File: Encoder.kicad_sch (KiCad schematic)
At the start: 6 parts, among them J2 ABZ encoder, J3 I2C ENCODER, J4 Conn_01x06_Male, J5 ANALOG ENCODER, U3 AS5055A

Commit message: finished routing
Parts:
- removed U3: AS5055A, Package_DFN_QFN:QFN-16-1EP_4x4mm_P0.65mm_EP2.7x2.7mm_PullBack, symbol Sensor_Magnetic:AS5055A
- added U3: AS5048B, Package_SO:TSSOP-14_4.4x5mm_P0.65mm, symbol Sensor_Magnetic:AS5048B
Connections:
- net +3.3V: now also U3.11 (VDD5V), U3.12 (VDD3V)
- net A: now also J2.5 (Pin_5); no longer J2.3 (Pin_3)
- net GND: now also U3.13 (GND), U3.3 (A2), U3.4 (A1)
- net I2C_SCL: now also J3.3 (Pin_3), U3.2 (SCL); no longer J3.4 (Pin_4)
- net I2C_SDA: now also J3.4 (Pin_4), U3.1 (SDA); no longer J3.3 (Pin_3)
- net Z: now also J2.3 (Pin_3); no longer J2.5 (Pin_5)
- new net ENC_PWM: U3.14 (PWM)
- no-connect marks 0 -> 6
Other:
- moved on the sheet: C32

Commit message: Routing done
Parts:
- added R11, R12: 10K, Resistor_SMD:R_0402_1005Metric, symbol Device:R
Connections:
- net +3.3V: now also R11.2, R12.2
- net I2C_SCL: now also R11.1
- net I2C_SDA: now also R12.1
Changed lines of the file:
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@@
     (effects (font (size 1.27 1.27)) (justify left))
   )
+  (hierarchical_label "I2C_SDA" (shape output) (at 159.766 160.274 180)
+    (effects (font (size 1.27 1.27)) (justify right))
+  )
   (hierarchical_label "ANALOG" (shape output) (at 126.238 47.244 270)
     (effects (font (size 1.27 1.27)) (justify right))
@@
     (effects (font (size 1.27 1.27)) (justify right))
   )
+  (hierarchical_label "I2C_SCL" (shape output) (at 159.766 157.734 180)
+    (effects (font (size 1.27 1.27)) (justify right))
+  )
   (hierarchical_label "I2C_SDA" (shape output) (at 87.122 66.04 270)
     (effects (font (size 1.27 1.27)) (justify right))
@@
   (hierarchical_label "SPI_CS" (shape input) (at 92.71 89.154 270)
     (effects (font (size 1.27 1.27)) (justify right))
+  )
+  (symbol (lib_id "Device:R") (at 163.576 157.734 90) (unit 1)
+    (in_bom yes) (on_board yes)
+    (property "Reference" "R11" (id 0) (at 164.338 157.988 90)
+      (effects (font (size 1.27 1.27)) (justify left))
+    )
+    (property "Value" "10K" (id 1) (at 165.1 155.956 90)
+      (effects (font (size 1.27 1.27)) (justify left))
+    )
+    (property "Footprint" "Resistor_SMD:R_0402_1005Metric" (id 2) (at 163.576 159.512 90)
+      (effects (font (size 1.27 1.27)) hide)
+    )
+    (property "Datasheet" "~" (id 3) (at 163.576 157.734 0)
+      (effects (font (size 1.27 1.27)) hide)
+    )
+    (pin "1")
+    (pin "2")
   )
   (symbol (lib_id "power:GND") (at 182.372 119.126 0) (unit 1)
@@
     (pin "2")
   )
+  (symbol (lib_id "Device:R") (at 163.576 160.274 90) (unit 1)
+    (in_bom yes) (on_board yes)
+    (property "Reference" "R12" (id 0) (at 164.338 160.528 90)
+      (effects (font (size 1.27 1.27)) (justify left))
+    )
+    (property "Value" "10K" (id 1) (at 164.846 162.052 90)
+      (effects (font (size 1.27 1.27)) (justify left))
+    )
+    (property "Footprint" "Resistor_SMD:R_0402_1005Metric" (id 2) (at 163.576 162.052 90)
+      (effects (font (size 1.27 1.27)) hide)
+    )
+    (property "Datasheet" "~" (id 3) (at 163.576 160.274 0)
+      (effects (font (size 1.27 1.27)) hide)
+    )
+    (pin "1")
+    (pin "2")
+  )
   (symbol (lib_id "power:GND") (at 167.386 125.476 270) (unit 1)
     (in_bom yes) (on_board yes) (fields_autoplaced)
@@
     )
     (property "Datasheet" "" (id 3) (at 97.79 89.154 0)
+      (effects (font (size 1.27 1.27)) hide)
+    )
+    (pin "1")
+  )
+  (symbol (lib_id "power:+3.3V") (at 167.386 157.734 270) (unit 1)
+    (in_bom yes) (on_board yes) (fields_autoplaced)
+    (property "Reference" "#PWR0126" (id 0) (at 163.576 157.734 0)
+      (effects (font (size 1.27 1.27)) hide)
+    )
+    (property "Value" "+3.3V" (id 1) (at 171.45 157.7339 90)
+      (effects (font (size 1.27 1.27)) (justify left))
+    )
+    (property "Footprint" "" (id 2) (at 167.386 157.734 0)
+      (effects (font (size 1.27 1.27)) hide)
+    )
+    (property "Datasheet" "" (id 3) (at 167.386 157.734 0)
       (effects (font (size 1.27 1.27)) hide)
     )
@@
       (effects (font (size 1.27 1.27)) hide)
     )
+    (pin "1")
+  )
+  (symbol (lib_id "power:+3.3V") (at 167.386 160.274 270) (unit 1)
+    (in_bom yes) (on_board yes) (fields_autoplaced)
+    (property "Reference" "#PWR0127" (id 0) (at 163.576 160.274 0)
+      (effects (font (size 1.27 1.27)) hide)
+    )
+    (property "Value" "+3.3V" (id 1) (at 171.45 160.2739 90)
+      (effects (font (size 1.27 1.27)) (justify left))
+    )
+    (property "Footprint" "" (id 2) (at 167.386 160.274 0)
+      (effects (font (size 1.27 1.27)) hide)
+    )
+    (property "Datasheet" "" (id 3) (at 167.386 160.274 0)
+      (effects (font (size 1.27 1.27)) hide)
+    )

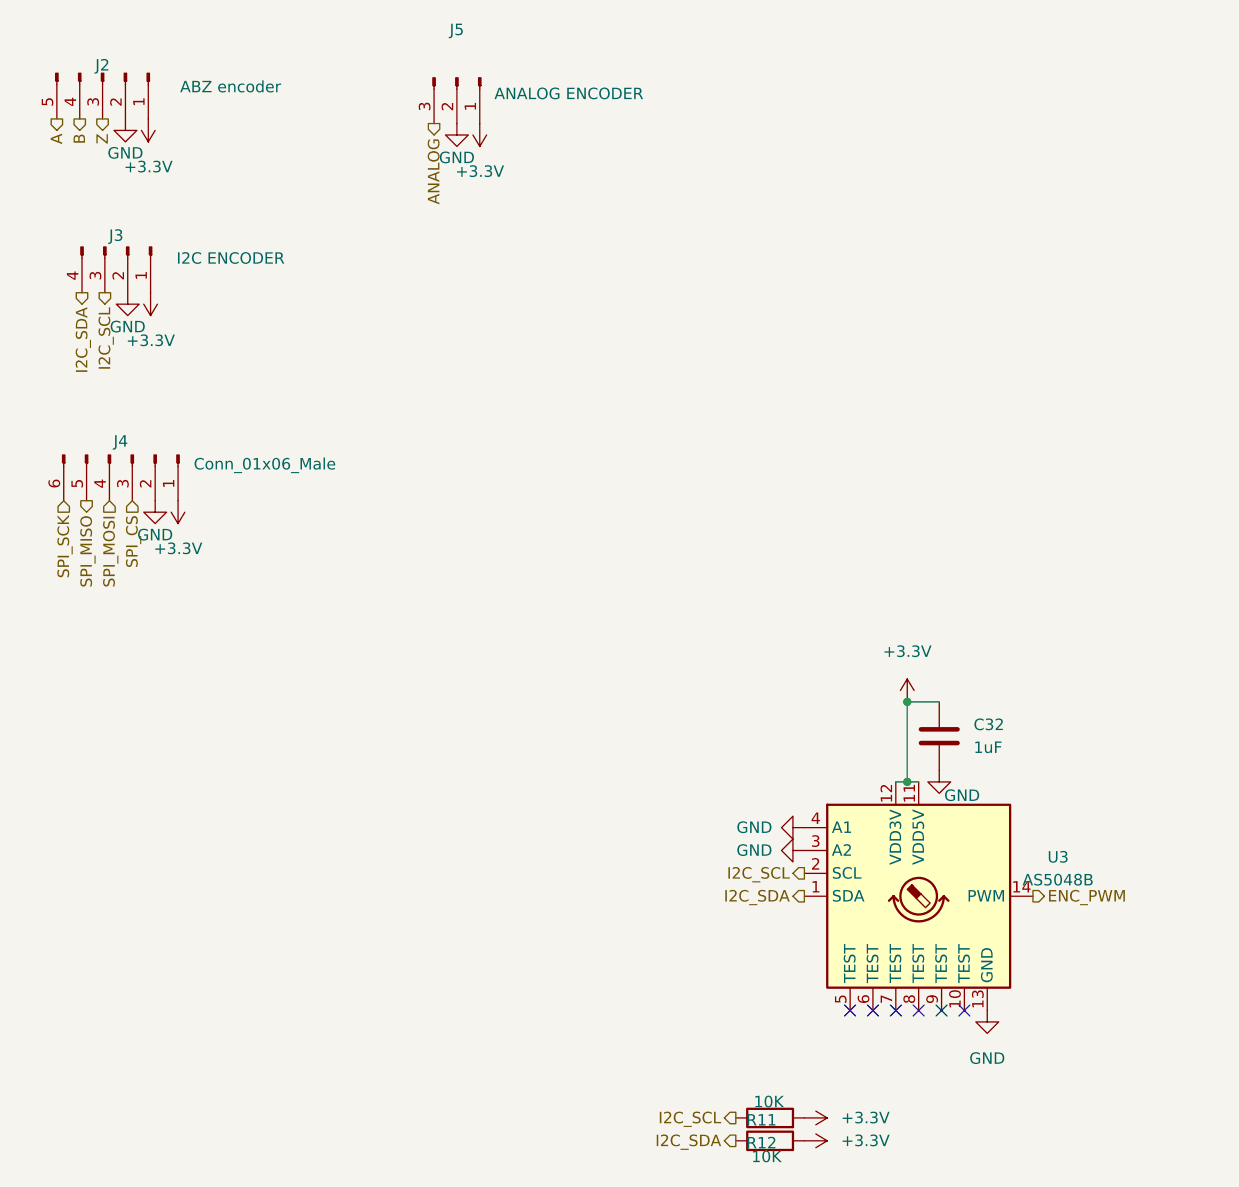
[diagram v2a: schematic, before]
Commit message: Using DRV8353 with built in current sense
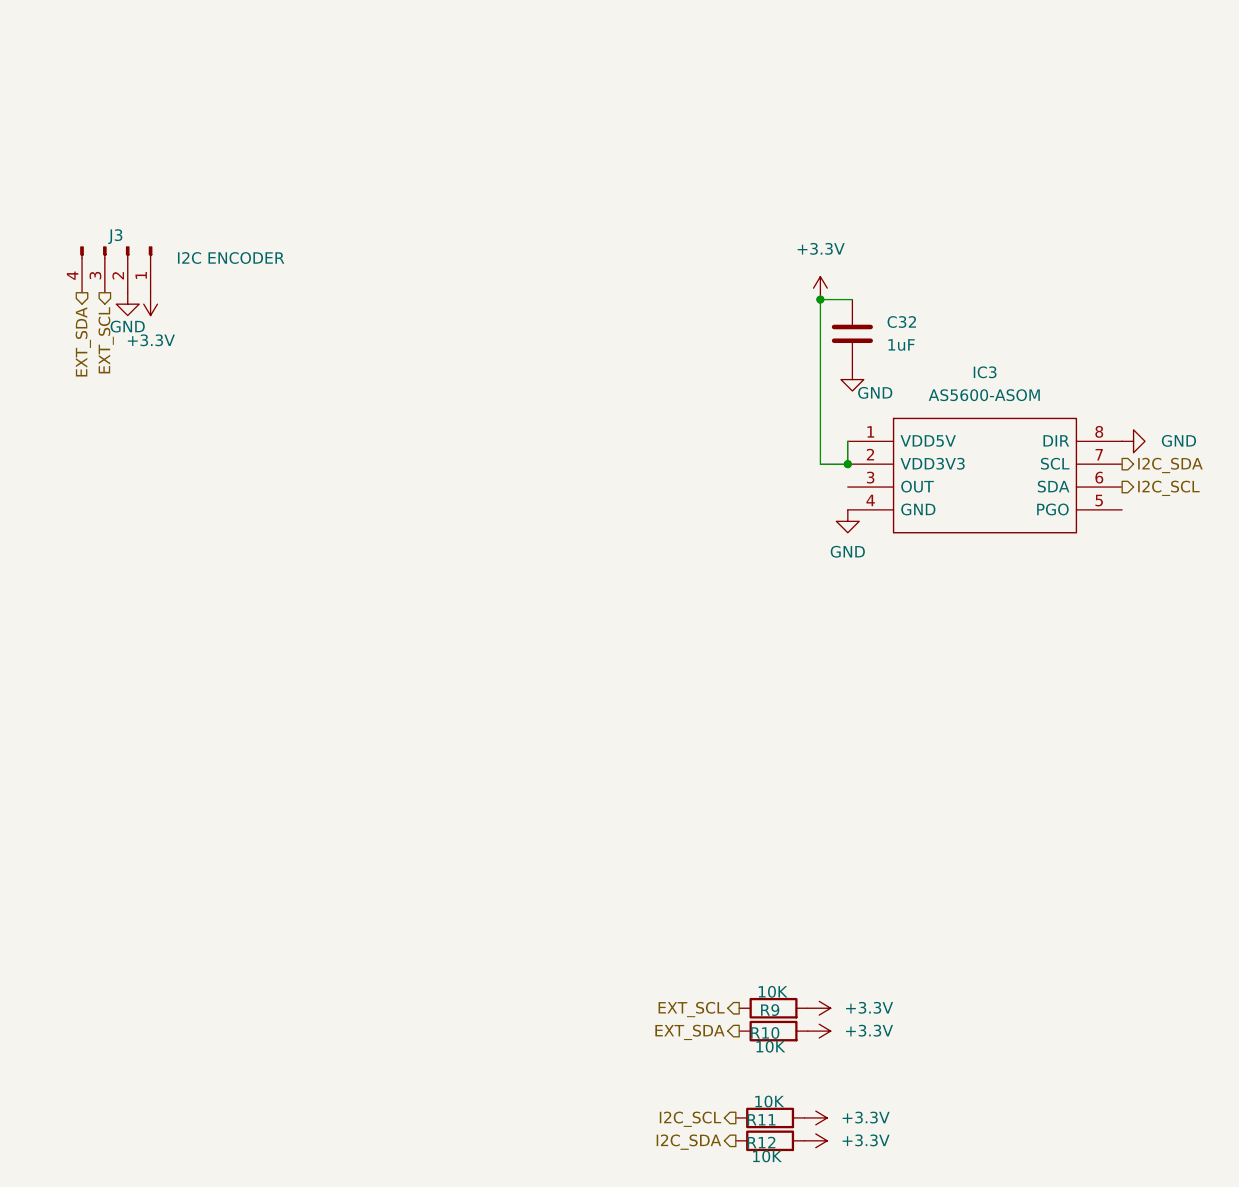
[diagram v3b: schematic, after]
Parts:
- removed J2: ABZ encoder, Connector_JST:JST_PH_B5B-PH-K_1x05_P2.00mm_Vertical, symbol Connector:Conn_01x05_Male
- removed J4: Conn_01x06_Male, Connector_JST:JST_PH_B6B-PH-K_1x06_P2.00mm_Vertical, symbol Connector:Conn_01x06_Male
- removed J5: ANALOG ENCODER, Connector_JST:JST_PH_B3B-PH-K_1x03_P2.00mm_Vertical, symbol Connector:Conn_01x03_Male
- removed U3: AS5048B, Package_SO:TSSOP-14_4.4x5mm_P0.65mm, symbol Sensor_Magnetic:AS5048B
- added IC3: AS5600-ASOM, AS5600:SOIC127P600X175-8N, symbol AS5600-ASOM:AS5600-ASOM
- added R10, R9: 10K, Resistor_SMD:R_0402_1005Metric, symbol Device:R
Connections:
- net +3.3V: now also IC3.1 (VDD5V), IC3.2 (VDD3V3), R10.2, R9.2
- net GND: now also IC3.4 (GND), IC3.8 (DIR)
- net I2C_SCL: now also IC3.6 (SDA); no longer J3.3 (Pin_3)
- net I2C_SDA: now also IC3.7 (SCL); no longer J3.4 (Pin_4)
- new net EXT_SCL: J3.3 (Pin_3), R9.1
- new net EXT_SDA: J3.4 (Pin_4), R10.1
- no-connect marks 6 -> 0
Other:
- moved on the sheet: C32

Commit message: init routing done
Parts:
- removed C32: 1uF, Capacitor_SMD:C_0402_1005Metric, symbol Device:C
- removed IC3: AS5600-ASOM, AS5600:SOIC127P600X175-8N, symbol AS5600-ASOM:AS5600-ASOM
- removed J3: I2C ENCODER, Connector_JST:JST_PH_B4B-PH-K_1x04_P2.00mm_Vertical, symbol Connector:Conn_01x04_Male
- removed R10, R11, R12, R9: 10K, Resistor_SMD:R_0402_1005Metric, symbol Device:R
- added J2: Conn_01x05_Female, Connector_Molex:Molex_PicoBlade_53398-0571_1x05-1MP_P1.25mm_Vertical, symbol Connector:Conn_01x05_Female
- added J4: Conn_01x04_Pin, Connector_Molex:Molex_PicoBlade_53398-0471_1x04-1MP_P1.25mm_Vertical, symbol Connector:Conn_01x04_Pin
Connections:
- net +3.3V: now also J2.2 (Pin_2), J4.3 (Pin_3)
- net I2C_SCL: now also J4.1 (Pin_1)
- net I2C_SDA: now also J4.2 (Pin_2)
- new net GNDD: J2.1 (Pin_1), J4.4 (Pin_4)
- new net U: J2.3 (Pin_3)
- new net V: J2.4 (Pin_4)
- new net W: J2.5 (Pin_5)
